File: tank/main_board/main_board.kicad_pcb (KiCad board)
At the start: 2 copper layers, 66.5 x 49.9 mm, 187 parts, among them J1 PowerIn, J10 Sonar2, J11 Programming Header, J12 SigOut, J16 PowerOut, J2 M2, J3 M1, J4 LEDs, J5 M3, J6 Spk, J7 Hall2, J8 Hall1, J9 Sonar1, Q1 2N3904, U1 L7805, U2 ATMEGA328P-PU, U3 SN74HC595, U4 TB6612FNG, U5 TB6612FNG, Y1 Crystal

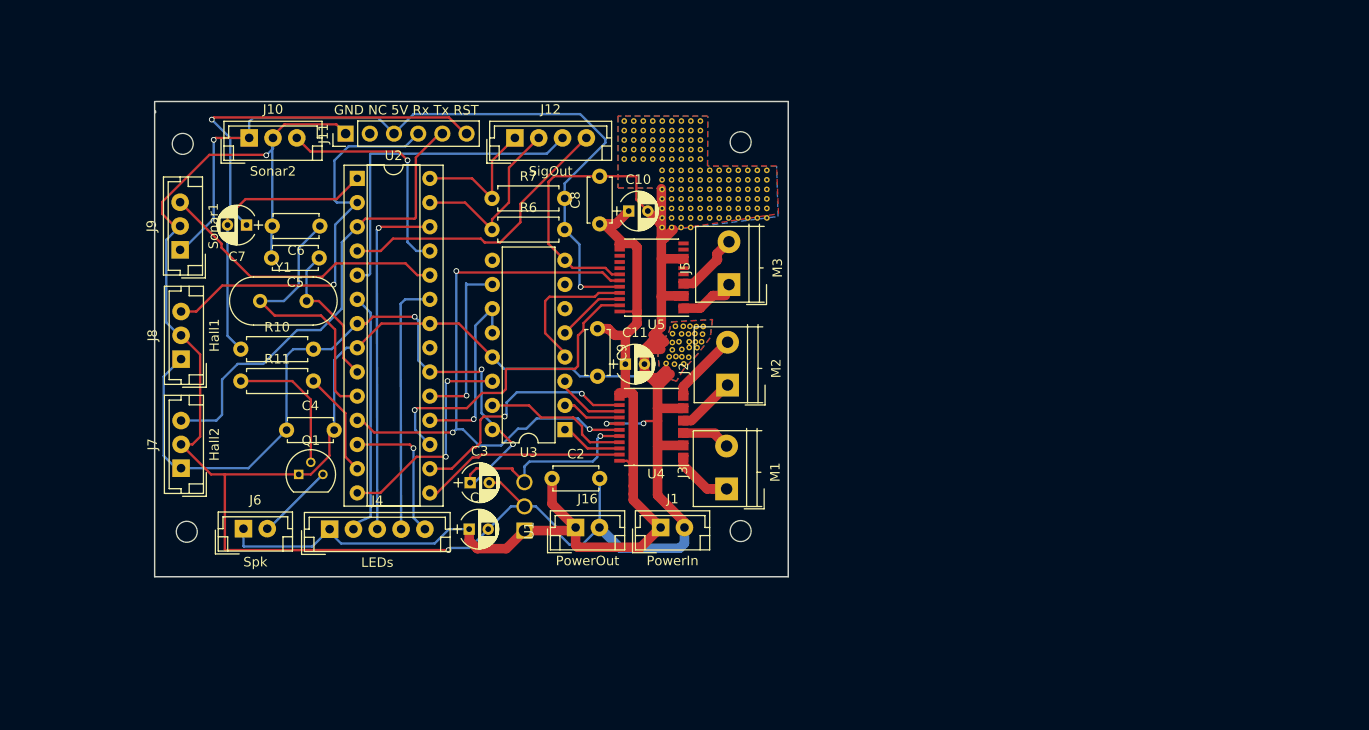
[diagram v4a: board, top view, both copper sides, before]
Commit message: tank main board version 0.5: - separate power supplies - sonar connectors are now bump encoders - removed PWN line for turret motor
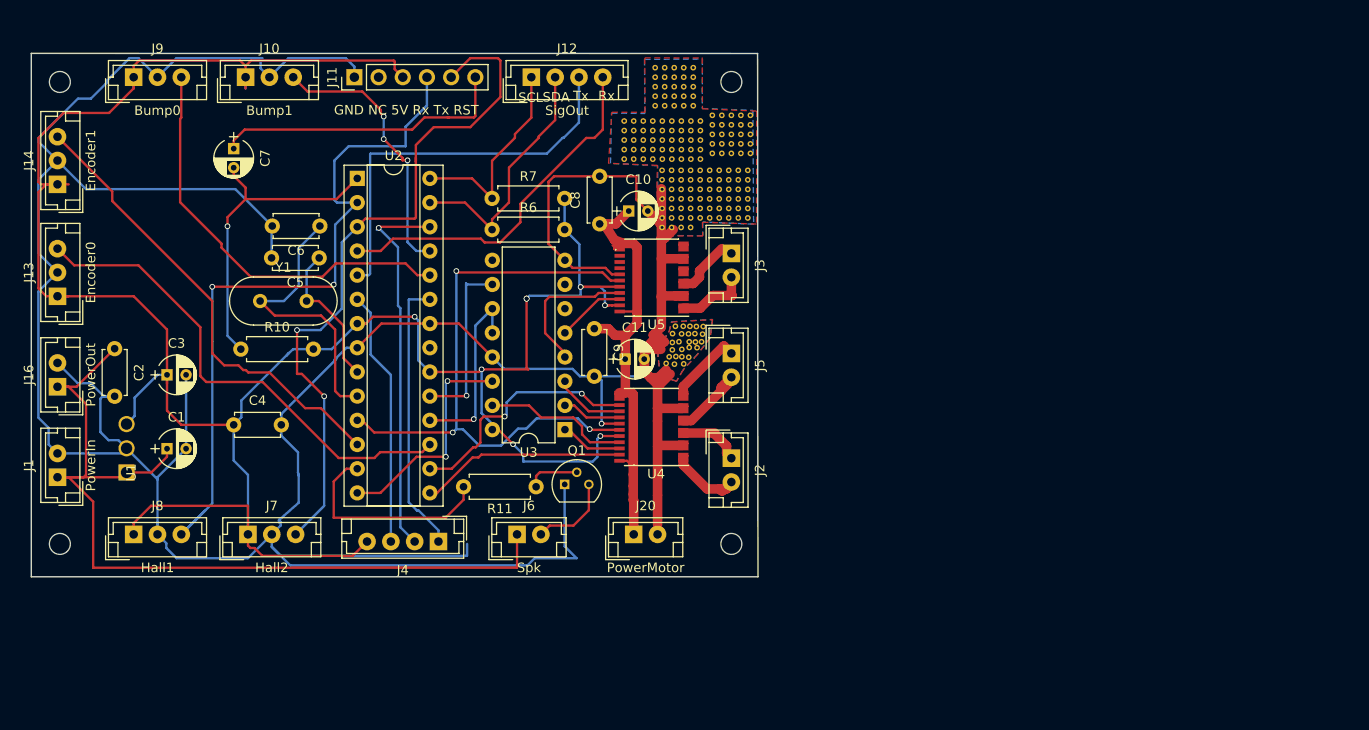
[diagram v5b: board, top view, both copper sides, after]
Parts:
- removed the REF** at (168.7, 91.8)
- removed the REF** at (167.7, 91.8)
- removed the REF** at (168.7, 90.8)
- removed the REF** at (167.7, 90.8)
- removed the REF** at (168.7, 89.8)
- removed the REF** at (167.7, 89.8)
- removed the REF** at (168.7, 88.8)
- removed the REF** at (167.7, 88.8)
- removed the REF** at (168.7, 87.8)
- removed the REF** at (167.7, 87.8)
- removed the REF** at (168.7, 86.8)
- removed the REF** at (167.7, 86.8)
- added J13: Encoder0, JST:JST_EH_B03B-EH-A_03x2.50mm_Straight, F.Cu at (94.2, 100.0)
- added J14: Encoder1, JST:JST_EH_B03B-EH-A_03x2.50mm_Straight, F.Cu at (94.2, 88.2)
- added J20: PowerMotor, JST:JST_EH_B02B-EH-A_02x2.50mm_Straight, F.Cu at (154.8, 125.0)
- added REF**: VIA-0.6mm, modules:VIA-0.6mm, F.Cu at (167.0, 85.0)
- added REF**: VIA-0.6mm, modules:VIA-0.6mm, F.Cu at (163.0, 84.0)
- added REF**: VIA-0.6mm, modules:VIA-0.6mm, F.Cu at (167.0, 83.0)
- added REF**: VIA-0.6mm, modules:VIA-0.6mm, F.Cu at (166.0, 83.0)
- added REF**: VIA-0.6mm, modules:VIA-0.6mm, F.Cu at (165.0, 83.0)
- added REF**: VIA-0.6mm, modules:VIA-0.6mm, F.Cu at (164.0, 83.0)
- added REF**: VIA-0.6mm, modules:VIA-0.6mm, F.Cu at (163.0, 83.0)
- added REF**: VIA-0.6mm, modules:VIA-0.6mm, F.Cu at (167.0, 82.0)
- added REF**: VIA-0.6mm, modules:VIA-0.6mm, F.Cu at (166.0, 82.0)
- added REF**: VIA-0.6mm, modules:VIA-0.6mm, F.Cu at (165.0, 82.0)
- added REF**: VIA-0.6mm, modules:VIA-0.6mm, F.Cu at (164.0, 82.0)
- added REF**: VIA-0.6mm, modules:VIA-0.6mm, F.Cu at (166.0, 85.0)
- added REF**: VIA-0.6mm, modules:VIA-0.6mm, F.Cu at (163.0, 82.0)
- added REF**: VIA-0.6mm, modules:VIA-0.6mm, F.Cu at (167.0, 81.0)
- added REF**: VIA-0.6mm, modules:VIA-0.6mm, F.Cu at (166.0, 81.0)
- added REF**: VIA-0.6mm, modules:VIA-0.6mm, F.Cu at (165.0, 81.0)
- added REF**: VIA-0.6mm, modules:VIA-0.6mm, F.Cu at (164.0, 81.0)
- added REF**: VIA-0.6mm, modules:VIA-0.6mm, F.Cu at (163.0, 81.0)
- added REF**: VIA-0.6mm, modules:VIA-0.6mm, F.Cu at (161.0, 80.0)
- added REF**: VIA-0.6mm, modules:VIA-0.6mm, F.Cu at (160.0, 80.0)
- added REF**: VIA-0.6mm, modules:VIA-0.6mm, F.Cu at (159.0, 80.0)
- added REF**: VIA-0.6mm, modules:VIA-0.6mm, F.Cu at (158.0, 80.0)
- added REF**: VIA-0.6mm, modules:VIA-0.6mm, F.Cu at (165.0, 85.0)
- added REF**: VIA-0.6mm, modules:VIA-0.6mm, F.Cu at (157.0, 80.0)
- added REF**: VIA-0.6mm, modules:VIA-0.6mm, F.Cu at (161.0, 79.0)
- added REF**: VIA-0.6mm, modules:VIA-0.6mm, F.Cu at (160.0, 79.0)
- added REF**: VIA-0.6mm, modules:VIA-0.6mm, F.Cu at (159.0, 79.0)
- added REF**: VIA-0.6mm, modules:VIA-0.6mm, F.Cu at (158.0, 79.0)
- added REF**: VIA-0.6mm, modules:VIA-0.6mm, F.Cu at (157.0, 79.0)
- added REF**: VIA-0.6mm, modules:VIA-0.6mm, F.Cu at (161.0, 78.0)
- added REF**: VIA-0.6mm, modules:VIA-0.6mm, F.Cu at (160.0, 78.0)
- added REF**: VIA-0.6mm, modules:VIA-0.6mm, F.Cu at (159.0, 78.0)
- added REF**: VIA-0.6mm, modules:VIA-0.6mm, F.Cu at (158.0, 78.0)
- added REF**: VIA-0.6mm, modules:VIA-0.6mm, F.Cu at (164.0, 85.0)
- added REF**: VIA-0.6mm, modules:VIA-0.6mm, F.Cu at (157.0, 78.0)
- added REF**: VIA-0.6mm, modules:VIA-0.6mm, F.Cu at (161.0, 77.0)
- added REF**: VIA-0.6mm, modules:VIA-0.6mm, F.Cu at (160.0, 77.0)
- added REF**: VIA-0.6mm, modules:VIA-0.6mm, F.Cu at (159.0, 77.0)
- added REF**: VIA-0.6mm, modules:VIA-0.6mm, F.Cu at (158.0, 77.0)
- added REF**: VIA-0.6mm, modules:VIA-0.6mm, F.Cu at (157.0, 77.0)
- added REF**: VIA-0.6mm, modules:VIA-0.6mm, F.Cu at (161.0, 76.0)
- added REF**: VIA-0.6mm, modules:VIA-0.6mm, F.Cu at (160.0, 76.0)
- added REF**: VIA-0.6mm, modules:VIA-0.6mm, F.Cu at (159.0, 76.0)
- added REF**: VIA-0.6mm, modules:VIA-0.6mm, F.Cu at (158.0, 76.0)
- added REF**: VIA-0.6mm, modules:VIA-0.6mm, F.Cu at (163.0, 85.0)
- added REF**: VIA-0.6mm, modules:VIA-0.6mm, F.Cu at (157.0, 76.0)
- added REF**: VIA-0.6mm, modules:VIA-0.6mm, F.Cu at (167.0, 84.0)
- added REF**: VIA-0.6mm, modules:VIA-0.6mm, F.Cu at (166.0, 84.0)
- added REF**: VIA-0.6mm, modules:VIA-0.6mm, F.Cu at (165.0, 84.0)
- added REF**: VIA-0.6mm, modules:VIA-0.6mm, F.Cu at (164.0, 84.0)
- J10: value Sonar2 -> Bump1
- J2: value M2 -> M1; footprint Custom:TerminalBlock_4UCON_19963_02x4.5mm_Straight -> JST:JST_EH_B02B-EH-A_02x2.50mm_Straight
- J3: value M1 -> M2; footprint Custom:TerminalBlock_4UCON_19963_02x4.5mm_Straight -> JST:JST_EH_B02B-EH-A_02x2.50mm_Straight
- J4: footprint Connectors_JST:JST_EH_B05B-EH-A_05x2.50mm_Straight -> JST:JST_EH_B04B-EH-A_04x2.50mm_Straight
- J5: value M3 -> M0; footprint Custom:TerminalBlock_4UCON_19963_02x4.5mm_Straight -> JST:JST_EH_B02B-EH-A_02x2.50mm_Straight
- J9: value Sonar1 -> Bump0
- U5: footprint Custom:TB6612FNGSINGLE -> Custom:TB6612FNG
- moved J1 63.5 mm to (94.2, 119.0), turned to 90 degrees
- moved J16 56.4 mm to (94.2, 109.5), turned to 90 degrees
- moved C2 47.9 mm to (100.2, 105.5), turned to 270 degrees
- moved G*** 44.0 mm to (107.8, 89.5)
- moved U1 42.2 mm to (101.5, 118.5)
- moved C3 33.8 mm to (105.8, 108.2)
- moved R11 32.9 mm to (144.5, 120.0), turned to 180 degrees
- moved C1 32.8 mm to (105.8, 116.0)
- moved J6 28.7 mm to (142.5, 125.0)
- moved Q1 27.9 mm to (147.5, 119.8)
- moved J3 24.7 mm to (165.0, 95.5), turned to 270 degrees
- moved J8 19.1 mm to (102.2, 125.0), turned to 0 degrees
- moved J9 18.8 mm to (102.2, 77.0), turned to 0 degrees
- moved REF** 14.4 mm to (94.5, 77.5)
- moved REF** 13.4 mm to (94.5, 126.0)
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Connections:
- net Sonar0 renamed Bump0
- net Sonar1 renamed Bump1
- C1 pad 1: 5V -> 9V
- C10 pad 1: 5V -> Vm
- C11 pad 1: 5V -> Vm
- C2 pad 1: 5V -> 9V
- C8 pad 1: 5V -> Vm
- C9 pad 1: 5V -> Vm
- J1 pad 1: 5V -> 9V
- J16 pad 1: 5V -> 9V
- J4 pad 1: 5V -> LED2
- J4 pad 2: LED0 -> LED1
- J4 pad 3: LED1 -> LED0
- J4 pad 4: LED2 -> 4.5V
- J6 pad 1: 5V -> 9V
- U1 pad 1: 5V -> 9V
- U2 pad 12: LED3 -> Encoder1
- U2 pad 17: M2PWM -> Encoder0
- U4 pad 1: Net-(J3-Pad1) -> Net-(J2-Pad2)
- U4 pad 11: Net-(J2-Pad2) -> Net-(J5-Pad1)
- U4 pad 12: Net-(J2-Pad2) -> Net-(J5-Pad1)
- U4 pad 13: 5V -> Vm
- U4 pad 14: 5V -> Vm
- U4 pad 2: Net-(J3-Pad1) -> Net-(J2-Pad2)
- U4 pad 24: 5V -> Vm
- U4 pad 5: Net-(J3-Pad2) -> Net-(J2-Pad1)
- U4 pad 6: Net-(J3-Pad2) -> Net-(J2-Pad1)
- U4 pad 7: Net-(J2-Pad1) -> Net-(J5-Pad2)
- U4 pad 8: Net-(J2-Pad1) -> Net-(J5-Pad2)
- U5 pad 1: Net-(J5-Pad1) -> Net-(J3-Pad2)
- U5 pad 13: 5V -> Vm
- U5 pad 14: 5V -> Vm
- U5 pad 2: Net-(J5-Pad1) -> Net-(J3-Pad2)
- U5 pad 23: M2PWM -> 4.5V
- U5 pad 24: 5V -> Vm
- U5 pad 5: Net-(J5-Pad2) -> Net-(J3-Pad1)
- U5 pad 6: Net-(J5-Pad2) -> Net-(J3-Pad1)
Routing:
- net 5V: track 107.0 -> 0.00 mm
- net 9V: track 0.00 -> 94.9 mm
- net GND: track 303.1 -> 391.3 mm, vias 4 -> 1
- net 4.5V: track 179.8 -> 255.9 mm, vias 6 -> 8
- net Encoder0: track 0.00 -> 51.8 mm
- net Vm: track 0.00 -> 50.1 mm
- net Encoder1: track 0.00 -> 48.7 mm
- net M2PWM: track 34.3 -> 0.00 mm, vias 1 -> 0
- net Hall0: track 43.5 -> 76.4 mm, vias 1 -> 2
- net Hall1: track 49.9 -> 74.6 mm, vias 0 -> 2
- net LED3: track 15.1 -> 0.00 mm, vias 1 -> 0
- net Bump0: track 30.8 -> 44.0 mm
- net SPK: track 11.1 -> 22.6 mm
- net Net-(Q1-Pad2): track 14.7 -> 5.56 mm
- net Net-(C7-Pad1): track 40.1 -> 31.5 mm, vias 1 -> 0
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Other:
- board size 66.5 x 49.9 mm -> 76.3 x 55 mm
- board text added: "Laser Tag Robot Tank Main Board v0.5 M.I.A.R. Labs nick.groesz@gmail.com"
- board text added: "Rx"
- board text added: "SCL"
- board text added: "SDA"
- board text added: "Tx"
- board text removed: "Laser Tag Robot Tank Main Board v0.4 M.I.A.R. Labs nick.groesz@gmail.com"

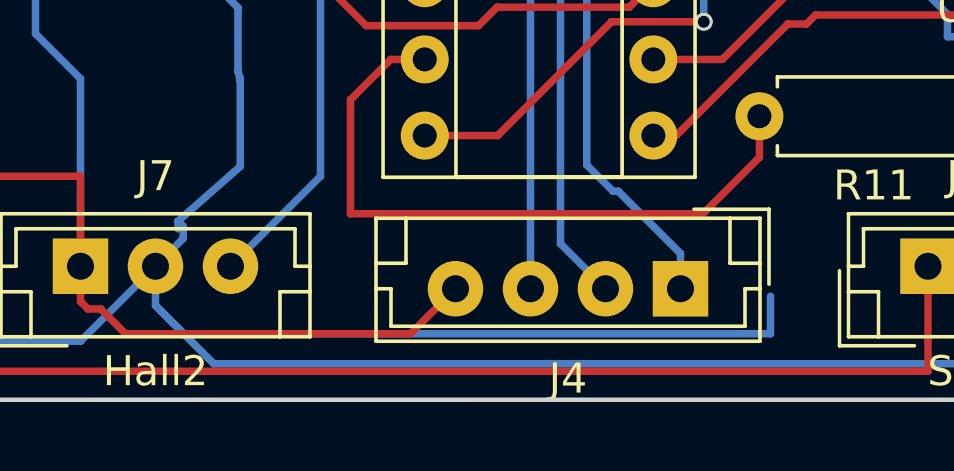
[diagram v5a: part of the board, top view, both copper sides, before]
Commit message: remove unused trace
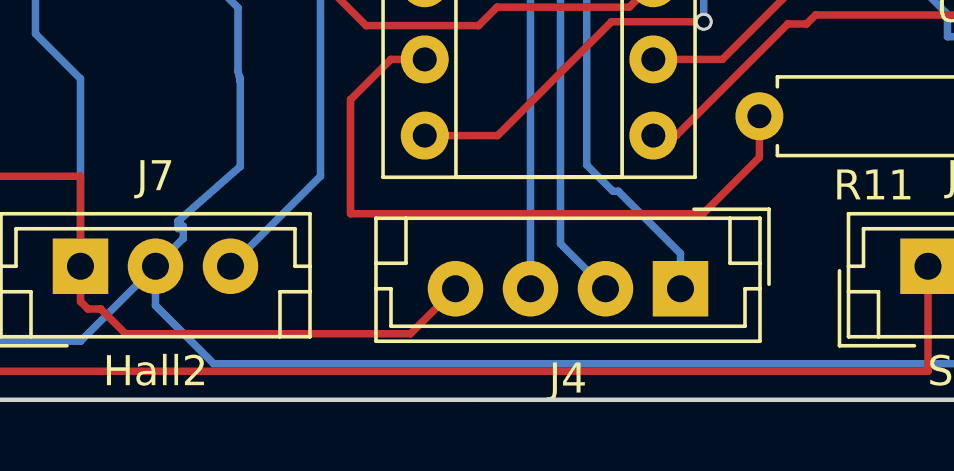
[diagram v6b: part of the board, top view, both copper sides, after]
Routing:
- net GND: track 391.3 -> 370.5 mm

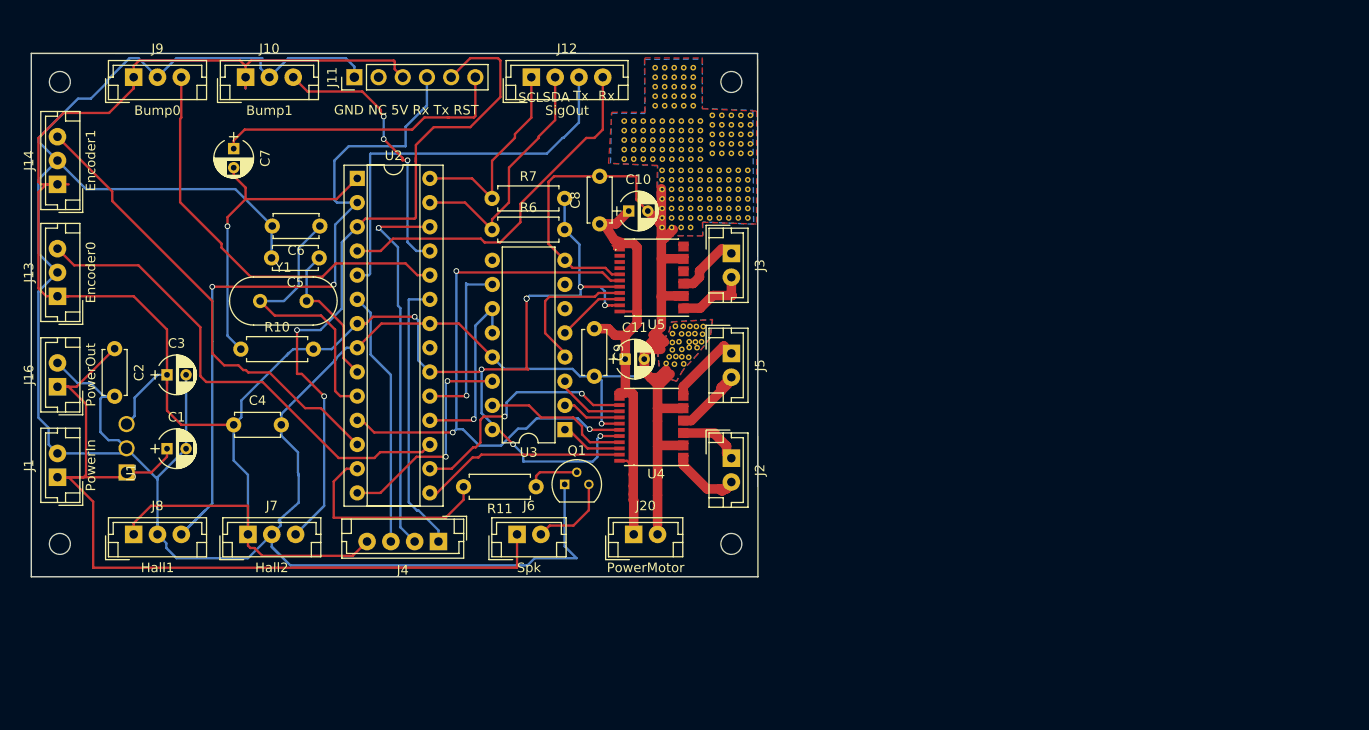
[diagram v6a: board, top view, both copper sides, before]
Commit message: Main Board version 0.6: - add ground planes on both layers - LED square is VCC - shorten board slightly - power out is regulated - vias. vias everywhere. - mounting holes embiggened
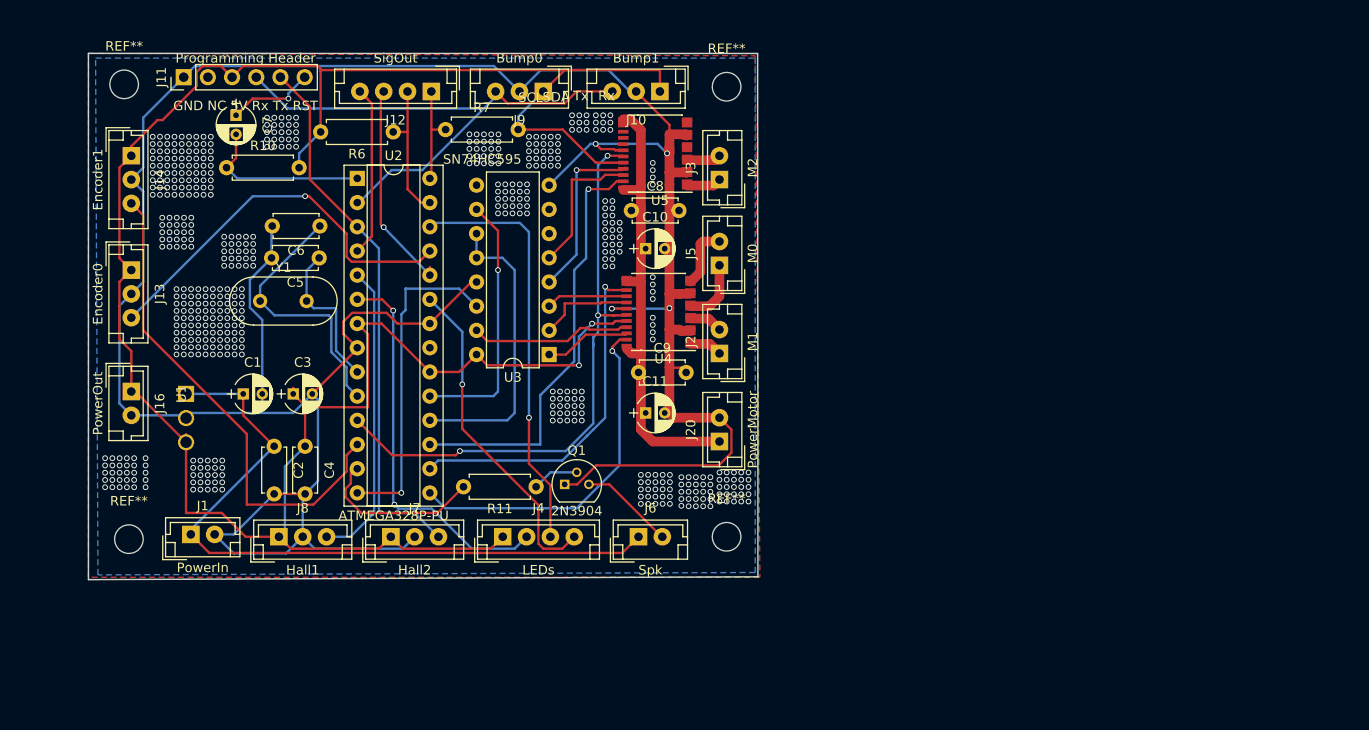
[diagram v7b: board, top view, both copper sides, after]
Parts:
- removed the REF** at (167.0, 85.0)
- removed the REF** at (163.0, 84.0)
- removed the REF** at (157.7, 90.8)
- removed the REF** at (166.7, 89.8)
- removed the REF** at (165.7, 89.8)
- removed the REF** at (164.7, 89.8)
- removed the REF** at (163.7, 89.8)
- removed the REF** at (162.7, 89.8)
- removed the REF** at (161.7, 89.8)
- removed the REF** at (160.7, 89.8)
- removed the REF** at (159.7, 89.8)
- removed the REF** at (158.7, 89.8)
- removed the REF** at (167.0, 83.0)
- removed the REF** at (157.7, 89.8)
- removed the REF** at (166.7, 88.8)
- removed the REF** at (165.7, 88.8)
- removed the REF** at (164.7, 88.8)
- removed the REF** at (163.7, 88.8)
- removed the REF** at (162.7, 88.8)
- removed the REF** at (161.7, 88.8)
- removed the REF** at (160.7, 88.8)
- removed the REF** at (159.7, 88.8)
- removed the REF** at (158.7, 88.8)
- removed the REF** at (166.0, 83.0)
- removed the REF** at (157.7, 88.8)
- removed the REF** at (166.7, 87.8)
- removed the REF** at (165.7, 87.8)
- removed the REF** at (164.7, 87.8)
- removed the REF** at (163.7, 87.8)
- removed the REF** at (162.7, 87.8)
- removed the REF** at (161.7, 87.8)
- removed the REF** at (160.7, 87.8)
- removed the REF** at (159.7, 87.8)
- removed the REF** at (158.7, 87.8)
- removed the REF** at (165.0, 83.0)
- removed the REF** at (157.7, 87.8)
- removed the REF** at (166.7, 86.8)
- removed the REF** at (165.7, 86.8)
- removed the REF** at (164.7, 86.8)
- removed the REF** at (163.7, 86.8)
- removed the REF** at (162.7, 86.8)
- removed the REF** at (161.7, 86.8)
- removed the REF** at (160.7, 86.8)
- removed the REF** at (159.7, 86.8)
- removed the REF** at (158.7, 86.8)
- removed the REF** at (164.0, 83.0)
- removed the REF** at (157.7, 86.8)
- removed the REF** at (161.8, 85.6)
- removed the REF** at (160.8, 85.6)
- removed the REF** at (159.8, 85.6)
- removed the REF** at (158.8, 85.6)
- removed the REF** at (157.8, 85.6)
- removed the REF** at (156.8, 85.6)
- removed the REF** at (155.8, 85.6)
- removed the REF** at (154.8, 85.6)
- removed the REF** at (153.8, 85.6)
- removed the REF** at (163.0, 83.0)
- removed the REF** at (161.8, 84.6)
- removed the REF** at (160.8, 84.6)
- removed the REF** at (159.8, 84.6)
- removed the REF** at (158.8, 84.6)
- removed the REF** at (157.8, 84.6)
- removed the REF** at (156.8, 84.6)
- removed the REF** at (155.8, 84.6)
- removed the REF** at (154.8, 84.6)
- removed the REF** at (153.8, 84.6)
- removed the REF** at (161.8, 83.6)
- removed the REF** at (167.0, 82.0)
- removed the REF** at (160.8, 83.6)
- removed the REF** at (159.8, 83.6)
- removed the REF** at (158.8, 83.6)
- removed the REF** at (157.8, 83.6)
- removed the REF** at (156.8, 83.6)
- removed the REF** at (155.8, 83.6)
- removed the REF** at (154.8, 83.6)
- removed the REF** at (153.8, 83.6)
- removed the REF** at (161.8, 82.6)
- removed the REF** at (160.8, 82.6)
- removed the REF** at (166.0, 82.0)
- removed the REF** at (159.8, 82.6)
- removed the REF** at (158.8, 82.6)
- removed the REF** at (157.8, 82.6)
- removed the REF** at (156.8, 82.6)
- removed the REF** at (155.8, 82.6)
- removed the REF** at (154.8, 82.6)
- removed the REF** at (153.8, 82.6)
- removed the REF** at (161.8, 81.6)
- removed the REF** at (160.8, 81.6)
- removed the REF** at (159.8, 81.6)
- removed the REF** at (165.0, 82.0)
- removed the REF** at (158.8, 81.6)
- removed the REF** at (157.8, 81.6)
- removed the REF** at (156.8, 81.6)
- removed the REF** at (155.8, 81.6)
- removed the REF** at (154.8, 81.6)
- removed the REF** at (94.5, 77.5)
- removed the REF** at (165.0, 77.5)
- removed the REF** at (165.0, 126.0)
- removed the REF** at (153.8, 81.6)
- removed the REF** at (159.1, 103.2)
- removed the REF** at (164.0, 82.0)
- removed the REF** at (166.0, 85.0)
- removed the REF** at (163.0, 82.0)
- removed the REF** at (167.0, 81.0)
- removed the REF** at (166.0, 81.0)
- removed the REF** at (165.0, 81.0)
- removed the REF** at (164.0, 81.0)
- removed the REF** at (163.0, 81.0)
- removed the REF** at (161.0, 80.0)
- removed the REF** at (160.0, 80.0)
- removed the REF** at (159.0, 80.0)
- removed the REF** at (158.0, 80.0)
- removed the REF** at (165.0, 85.0)
- removed the REF** at (157.0, 80.0)
- removed the REF** at (161.0, 79.0)
- removed the REF** at (160.0, 79.0)
- removed the REF** at (159.0, 79.0)
- removed the REF** at (158.0, 79.0)
- removed the REF** at (157.0, 79.0)
- removed the REF** at (161.0, 78.0)
- removed the REF** at (160.0, 78.0)
- removed the REF** at (159.0, 78.0)
- removed the REF** at (158.0, 78.0)
- removed the REF** at (164.0, 85.0)
- removed the REF** at (157.0, 78.0)
- removed the REF** at (161.0, 77.0)
- removed the REF** at (160.0, 77.0)
- removed the REF** at (159.0, 77.0)
- removed the REF** at (158.0, 77.0)
- removed the REF** at (157.0, 77.0)
- removed the REF** at (161.0, 76.0)
- removed the REF** at (160.0, 76.0)
- removed the REF** at (159.0, 76.0)
- removed the REF** at (158.0, 76.0)
- removed the REF** at (163.0, 85.0)
- removed the REF** at (157.0, 76.0)
- removed the REF** at (94.5, 126.0)
- removed the REF** at (158.2, 107.0)
- removed the REF** at (159.0, 107.1)
- removed the REF** at (160.0, 107.1)
- removed the REF** at (160.5, 106.4)
- removed the REF** at (159.8, 106.3)
- removed the REF** at (159.2, 106.3)
- removed the REF** at (158.5, 106.3)
- removed the REF** at (158.8, 105.6)
- removed the REF** at (167.0, 84.0)
- removed the REF** at (159.8, 105.6)
- removed the REF** at (160.6, 105.4)
- removed the REF** at (161.4, 105.4)
- removed the REF** at (161.9, 104.8)
- removed the REF** at (161.2, 104.8)
- removed the REF** at (160.6, 104.8)
- removed the REF** at (159.5, 104.8)
- removed the REF** at (158.8, 104.8)
- removed the REF** at (158.8, 103.9)
- removed the REF** at (159.8, 104.0)
- removed the REF** at (166.0, 84.0)
- removed the REF** at (160.5, 104.0)
- removed the REF** at (161.2, 103.9)
- removed the REF** at (162.0, 104.0)
- removed the REF** at (162.1, 103.2)
- removed the REF** at (161.3, 103.2)
- removed the REF** at (160.7, 103.2)
- removed the REF** at (159.9, 103.2)
- removed the REF** at (160.7, 92.8)
- removed the REF** at (159.7, 92.8)
- removed the REF** at (158.7, 92.8)
- removed the REF** at (165.0, 84.0)
- removed the REF** at (157.7, 92.8)
- removed the REF** at (166.7, 91.8)
- removed the REF** at (165.7, 91.8)
- removed the REF** at (164.7, 91.8)
- removed the REF** at (163.7, 91.8)
- removed the REF** at (162.7, 91.8)
- removed the REF** at (161.7, 91.8)
- removed the REF** at (160.7, 91.8)
- removed the REF** at (159.7, 91.8)
- removed the REF** at (158.7, 91.8)
- removed the REF** at (164.0, 84.0)
- removed the REF** at (157.7, 91.8)
- removed the REF** at (166.7, 90.8)
- removed the REF** at (165.7, 90.8)
- removed the REF** at (164.7, 90.8)
- removed the REF** at (163.7, 90.8)
- removed the REF** at (162.7, 90.8)
- removed the REF** at (161.7, 90.8)
- removed the REF** at (160.7, 90.8)
- removed the REF** at (159.7, 90.8)
- removed the REF** at (158.7, 90.8)
- added REF**: MountingHole_3mm, MountingHole:MountingHole_3mm, F.Cu at (101.2, 77.8)
- added REF**: MountingHole_3mm, MountingHole:MountingHole_3mm, F.Cu at (101.8, 125.5)
- added REF**: MountingHole_3mm, MountingHole:MountingHole_3mm, F.Cu at (164.5, 78.0)
- added REF**: MountingHole_3mm, MountingHole:MountingHole_3mm, F.Cu at (164.5, 125.2)
- moved G*** 46.4 mm to (146.8, 114.8)
- moved J10 43.5 mm to (157.5, 78.5), turned to 180 degrees
- moved J9 43.0 mm to (145.2, 78.5), turned to 180 degrees
- moved C2 19.6 mm to (117.0, 115.8)
- moved R10 19.1 mm to (112.0, 86.5)
- moved J11 17.9 mm to (107.5, 77.0)
- moved J8 15.3 mm to (117.5, 125.2)
- moved J1 15.2 mm to (108.2, 125.0), turned to 0 degrees
- moved J7 15.0 mm to (129.2, 125.2)
- moved R6 14.6 mm to (129.5, 82.8), turned to 180 degrees
- moved C3 13.4 mm to (119.0, 110.2)
- moved J20 13.3 mm to (163.8, 115.2), turned to 90 degrees
- moved U5 13.0 mm to (157.5, 85.0)
- moved J6 12.8 mm to (155.2, 125.2)
- moved U4 12.1 mm to (157.8, 101.6)
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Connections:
- net Hall1 renamed TurretCal
- J10 pad 3: Bump1 -> Bump
- J11 pad 4: Hall0 -> Bump
- J16 pad 1: 9V -> 4.5V
- J4 pad 1: LED2 -> 4.5V
- J4 pad 2: LED1 -> LED0
- J4 pad 3: LED0 -> LED1
- J4 pad 4: 4.5V -> LED2
- J8 pad 3: Hall0 -> TurretEncoder
- J9 pad 3: Bump0 -> Bump
- U2 pad 17: Encoder0 -> M2PWM
- U2 pad 2: Hall0 -> Bump
- U2 pad 24: Bump0 -> IRTx
- U2 pad 25: Bump1 -> Encoder0
- U2 pad 5: IRTx -> TurretEncoder
- U4 pad 1: Net-(J2-Pad2) -> Net-(J2-Pad1)
- U4 pad 11: Net-(J5-Pad1) -> Net-(J5-Pad2)
- U4 pad 12: Net-(J5-Pad1) -> Net-(J5-Pad2)
- U4 pad 2: Net-(J2-Pad2) -> Net-(J2-Pad1)
- U4 pad 5: Net-(J2-Pad1) -> Net-(J2-Pad2)
- U4 pad 6: Net-(J2-Pad1) -> Net-(J2-Pad2)
- U4 pad 7: Net-(J5-Pad2) -> Net-(J5-Pad1)
- U4 pad 8: Net-(J5-Pad2) -> Net-(J5-Pad1)
- U5 pad 1: Net-(J3-Pad2) -> Net-(J3-Pad1)
- U5 pad 12: Net-(U5-Pad12) -> Net-(U5-Pad11)
- U5 pad 2: Net-(J3-Pad2) -> Net-(J3-Pad1)
- U5 pad 23: 4.5V -> M2PWM
- U5 pad 5: Net-(J3-Pad1) -> Net-(J3-Pad2)
- U5 pad 6: Net-(J3-Pad1) -> Net-(J3-Pad2)
- U5 pad 8: Net-(U5-Pad8) -> Net-(U5-Pad7)
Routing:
- net Hall0: track 76.4 -> 0.00 mm, vias 2 -> 0
- net Bump: track 0.00 -> 58.2 mm
- net GND: track 370.5 -> 313.7 mm, vias 1 -> 520
- net M2PWM: track 0.00 -> 44.7 mm, vias 0 -> 1
- net Bump0: track 44.0 -> 0.00 mm
- net TurretEncoder: track 0.00 -> 31.7 mm
- net Bump1: track 28.7 -> 0.00 mm, vias 3 -> 0
- net Net-(C7-Pad1): track 31.5 -> 9.18 mm, vias 0 -> 1
- net 9V: track 94.9 -> 74.6 mm
- net IRTx: track 42.0 -> 22.8 mm, vias 0 -> 1
- net IRRx: track 38.0 -> 19.1 mm
- net TurretCal: track 74.6 -> 57.3 mm, vias 2 -> 0
- net Net-(C7-Pad2): track 33.6 -> 18.1 mm, vias 1 -> 0
- net M0PWM: track 21.6 -> 37.0 mm, vias 0 -> 1
- net LED0: track 26.9 -> 41.2 mm, vias 0 -> 2
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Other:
- board size 76.3 x 55 mm -> 70.3 x 55.2 mm
- board text added: "Laser Tag Robot Tank Main Board v0.6 M.I.A.R. Labs nick.groesz@gmail.com"
- board text removed: "Laser Tag Robot Tank Main Board v0.5 M.I.A.R. Labs nick.groesz@gmail.com"
